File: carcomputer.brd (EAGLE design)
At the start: 103.8 x 90.2 mm, 73 parts, among them IC1 LM358N, K1 351, K2 RT184012, K3 RT184012, Q1 BS170, Q5 TIP136, T1 BC618, T2 BC618, T3 BC618, T4 BC618

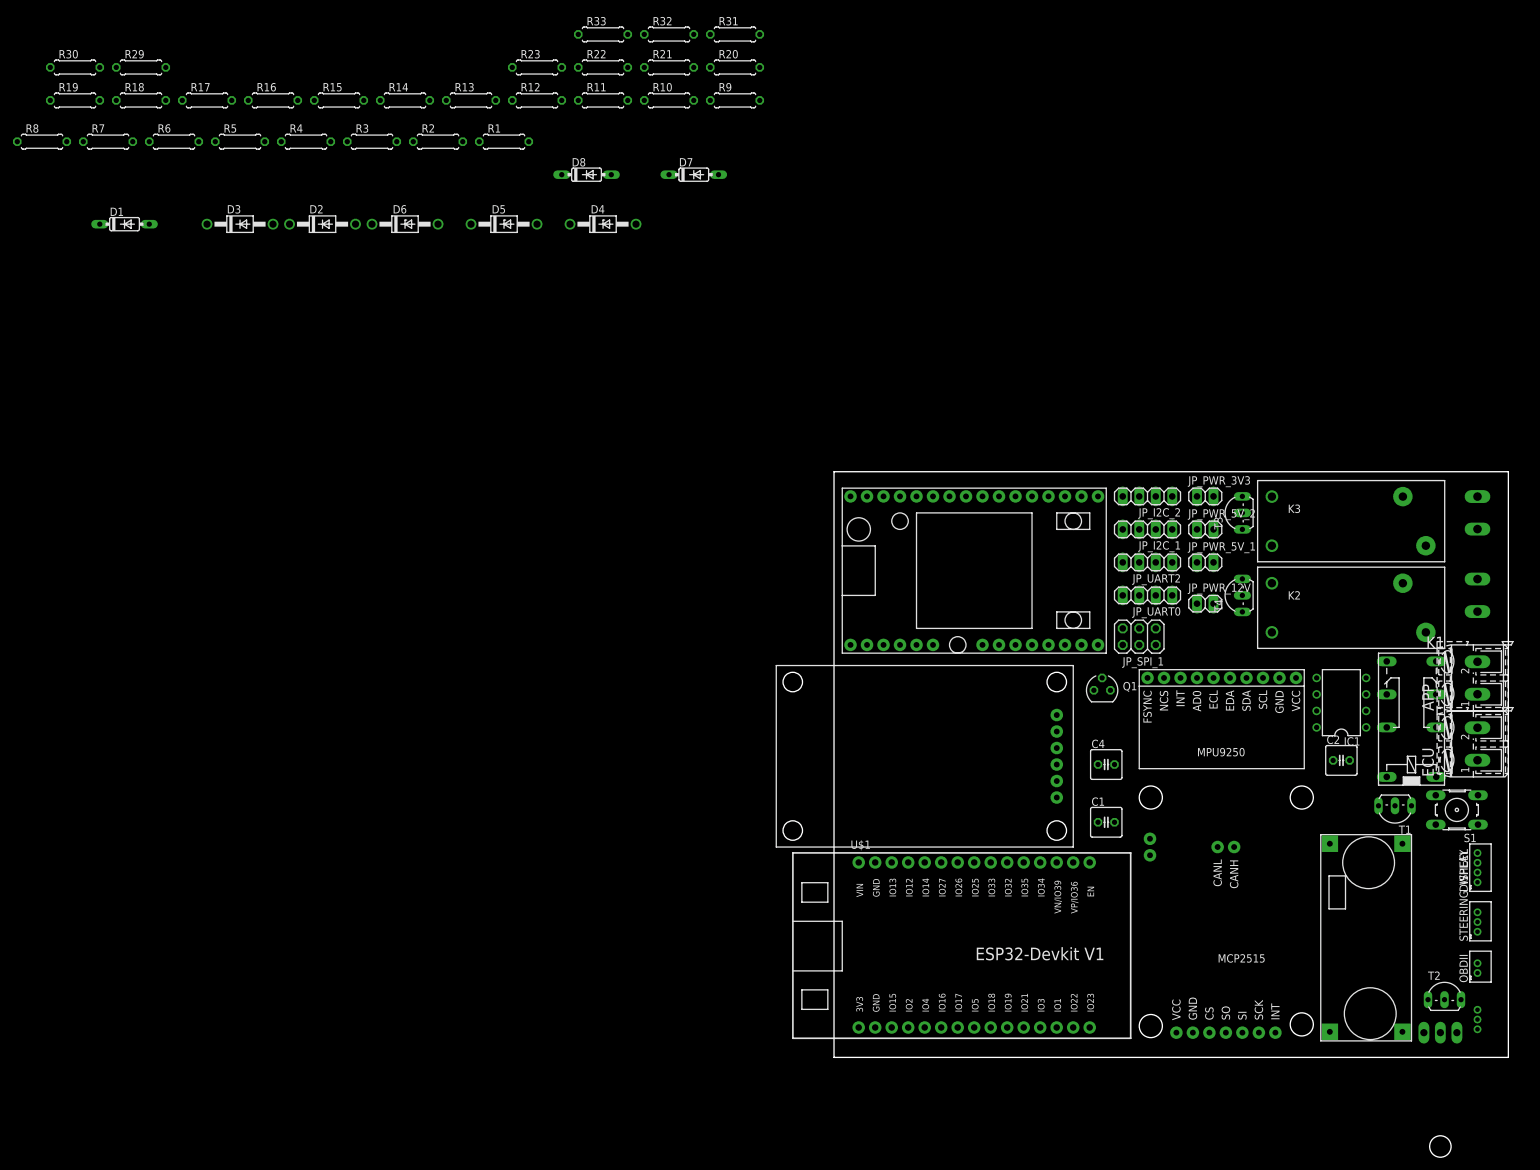
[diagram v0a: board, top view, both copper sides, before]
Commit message: Routed almost first complete single board
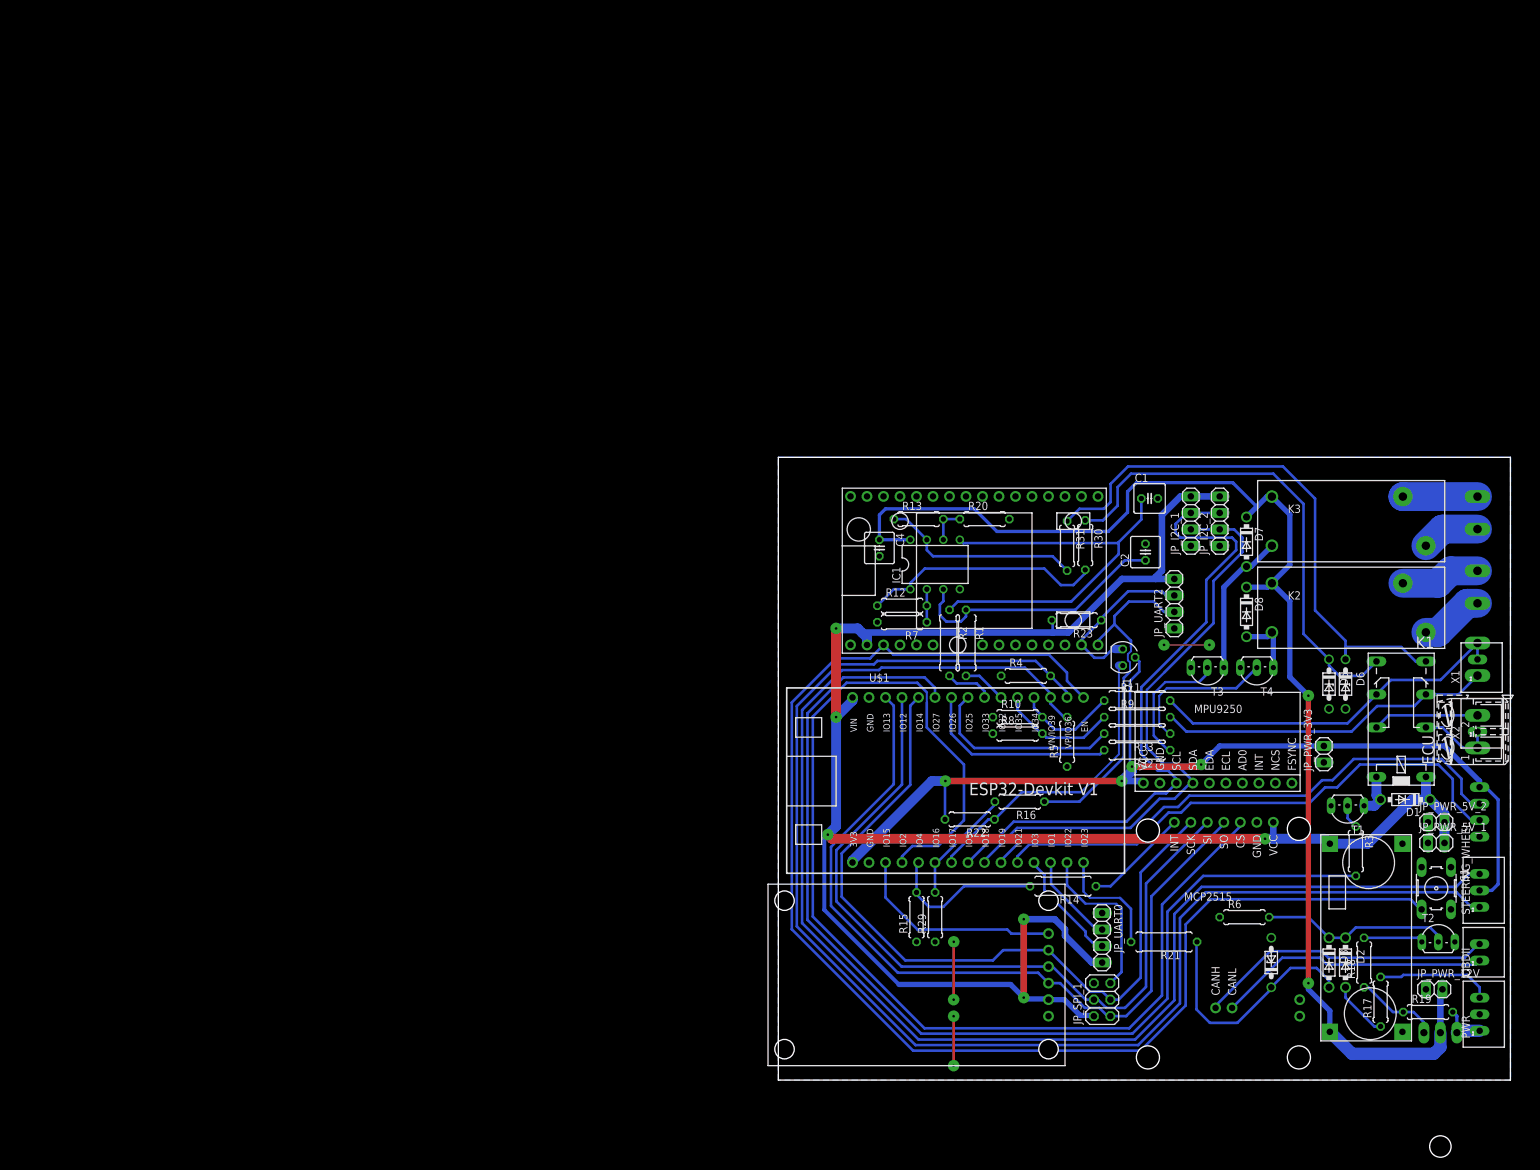
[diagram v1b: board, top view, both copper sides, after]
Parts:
- added X1, X2: 2.52B-ZR, con-jst-custom:B2B-ZR2.5
- D1, D7, D8: value 1N4148DO35-7 -> 1N40047; device diode:DO35-7 -> diode-custom:DO41-7.6
- D2, D3: value 1N4004 -> 1N40047; device diode:DO41-10 -> diode-custom:DO41-7.6
- D4, D5, D6: device diode:DO41Z10 -> diode-custom:DO41Z7.6
- DISPLAY: value B4B-ZR -> 2.54B-ZR; device con-jst-custom:B4B-ZR -> con-jst-custom:B4B-ZR2.5
- OBDII: value B2B-ZR -> 2.52B-ZR; device con-jst-custom:B2B-ZR -> con-jst-custom:B2B-ZR2.5
- PWR, STEERING_WHEEL: value B3B-ZR -> 2.53B-ZR; device con-jst-custom:B3B-ZR -> con-jst-custom:B3B-ZR2.5
- R1, R11, R14, R2, R21, R32, R33, R9: device rcl:0207/7 -> rcl:0309/10
- moved R19 251.1 mm to (88.9, 3.17)
- moved R18 230.4 mm to (79.1, 10.8), turned to 90 degrees
- moved R17 227.8 mm to (81.6, 4.76), turned to 90 degrees
- moved D1 216.2 mm to (85.4, 35.9), turned to 180 degrees
- moved R6 203.5 mm to (60.6, 17.8)
- moved D3 202.5 mm to (73.7, 10.8), turned to 270 degrees
- moved D2 194.2 mm to (76.2, 10.8), turned to 270 degrees
- moved R3 186.7 mm to (77.8, 27.9), turned to 270 degrees
- moved R29 179.0 mm to (13.0, 17.8), turned to 90 degrees
- moved R8 175.7 mm to (25.7, 46.0)
- moved R30 172.0 mm to (36.1, 75.1), turned to 270 degrees
- moved D6 161.2 mm to (76.2, 53.7), turned to 270 degrees
- moved R14 157.8 mm to (32.7, 22.5), turned to 180 degrees
- moved R16 157.7 mm to (26.0, 35.6), turned to 180 degrees
- moved R5 157.3 mm to (33.3, 44.8), turned to 90 degrees
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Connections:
- net +12V: now also PWR.1; no longer D7.C, D8.C, JP_PWR_12V.2, K2.A2, K3.A2, PWR.3
- net +3V3: now also DISPLAY.1; no longer DISPLAY.4
- net +5V: now also K1.1; no longer K1.16
- net APP_0_IN: now also X1.2
- net APP_1_IN: now also X1.1
- net BTN_0: now also R4.2, STEERING_WHEEL.1; no longer R5.2, STEERING_WHEEL.3
- net BTN_1: now also R5.2, STEERING_WHEEL.3; no longer R4.2, STEERING_WHEEL.1
- net GND: now also DISPLAY.4; no longer DISPLAY.1
- net GPS_RX: now also JP_UART2.3; no longer JP_UART2.2
- net GPS_TX: now also JP_UART2.2; no longer JP_UART2.3
- net I2C1_SCL: now also DISPLAY.2; no longer DISPLAY.3
- net I2C1_SDA: now also DISPLAY.3; no longer DISPLAY.2
- net IGNITION: now also PWR.3; no longer PWR.1
- net N$1: now also K1.16; no longer K1.1
- net N$6: now also K1.P2, X2.2; no longer K1.P1
- net N$7: now also K1.P1, X2.1; no longer K1.P2
- net PWR_IN+: now also D7.C, D8.C, JP_PWR_12V.2, K2.A2, K3.A2
- net UART0_RX: now also JP_UART0.3; no longer JP_UART0.2
- net UART0_TX: now also JP_UART0.2; no longer JP_UART0.3
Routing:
- net +5V: track 0.00 -> 314.1 mm, vias 0 -> 6
- net BTN_0: track 0.00 -> 212.2 mm
- net BTN_1: track 0.00 -> 210.4 mm
- net MCU_RESET: track 0.00 -> 209.9 mm
- net PWR_IN+: track 0.00 -> 200.7 mm, vias 0 -> 2
- net CAN_CS: track 0.00 -> 180.6 mm
- net APP_ENABLE: track 0.00 -> 165.4 mm
- net +3V3: track 0.00 -> 154.8 mm, vias 0 -> 4
- net SPI_MISO: track 0.00 -> 125.2 mm
- net SPI_MOSI: track 0.00 -> 120.6 mm
- net SPI_SCK: track 0.00 -> 118.0 mm
- net I2C0_SCL: track 0.00 -> 102.3 mm
- net I2C0_SDA: track 0.00 -> 93.7 mm
- net N$3: track 0.00 -> 87.2 mm
- net I2C1_SCL: track 0.00 -> 84.7 mm
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- added copper zone on layer 16, net GND
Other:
- board size 103.8 x 90.2 mm -> 112.7 x 95.9 mm

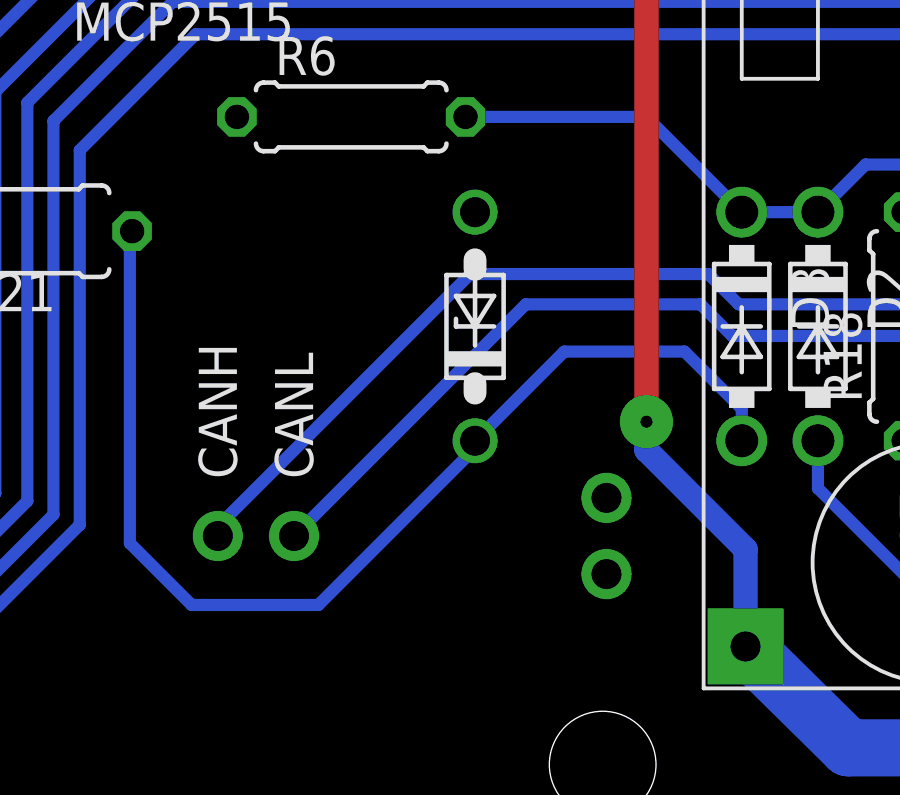
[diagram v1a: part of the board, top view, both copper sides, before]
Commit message: Added pinheaders connection for CAN terminator resistors
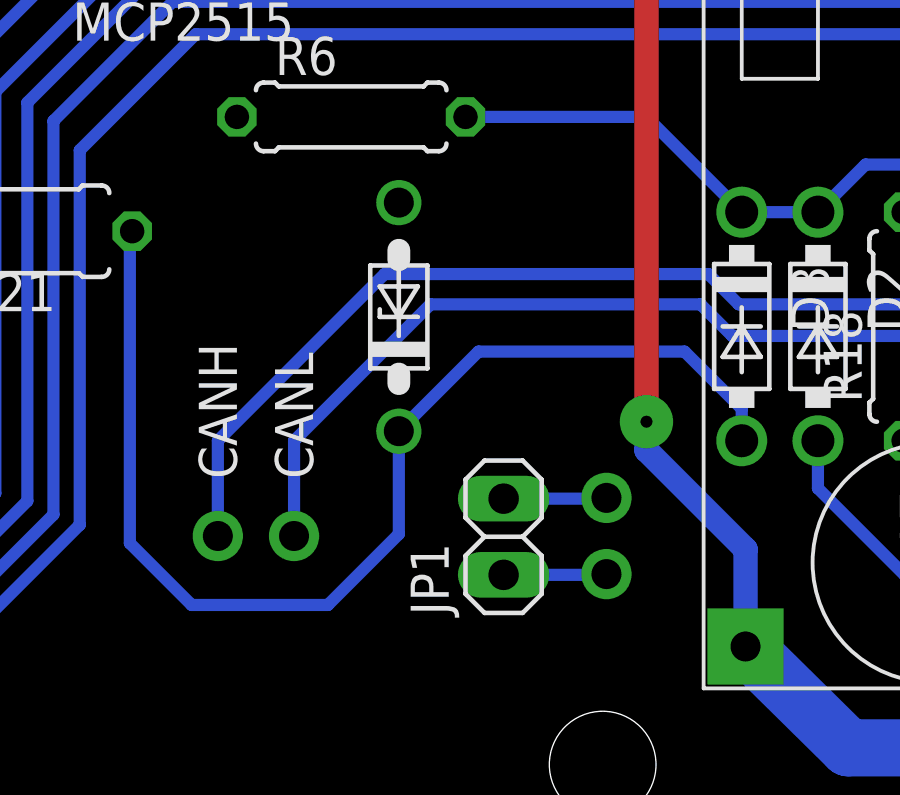
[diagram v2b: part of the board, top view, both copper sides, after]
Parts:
- added JP1: (no value), pinhead:1X02
- moved D4 2.56 mm to (62.2, 11.1)
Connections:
- new net CAN_TERM_RESTISTOR0: JP1.2, U$2.TERM_REST0
- new net CAN_TERM_RESTISTOR1: JP1.1, U$2.TERM_REST1
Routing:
- net CAN_TERM_RESTISTOR1: track 0.00 -> 3.44 mm
- net CAN_TERM_RESTISTOR0: track 0.00 -> 3.44 mm
- net CAN_L: track 42.0 -> 43.9 mm
- net N$11: track 37.2 -> 39.1 mm
- net CAN_H: track 45.7 -> 47.4 mm
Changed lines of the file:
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@@
 <setting verticaltext="up"/>
 </settings>
-<grid distance="4" unitdist="mil" unit="mil" style="lines" multiple="1" display="yes" altdistance="5" altunitdist="mil" altunit="mil"/>
+<grid distance="12.5" unitdist="mil" unit="mil" style="lines" multiple="1" display="yes" altdistance="5" altunitdist="mil" altunit="mil"/>
 <layers>
 <layer number="1" name="Top" color="4" fill="1" visible="yes" active="yes"/>
@@
 <layer number="19" name="Unrouted" color="6" fill="1" visible="yes" active="yes"/>
 <layer number="20" name="Dimension" color="24" fill="1" visible="no" active="yes"/>
-<layer number="21" name="tPlace" color="7" fill="1" visible="no" active="yes"/>
-<layer number="22" name="bPlace" color="7" fill="1" visible="no" active="yes"/>
-<layer number="23" name="tOrigins" color="15" fill="1" visible="no" active="yes"/>
-<layer number="24" name="bOrigins" color="15" fill="1" visible="no" active="yes"/>
-<layer number="25" name="tNames" color="7" fill="1" visible="no" active="yes"/>
-<layer number="26" name="bNames" color="7" fill="1" visible="no" active="yes"/>
-<layer number="27" name="tValues" color="7" fill="1" visible="no" active="yes"/>
-<layer number="28" name="bValues" color="7" fill="1" visible="no" active="yes"/>
+<layer number="21" name="tPlace" color="7" fill="1" visible="yes" active="yes"/>
+<layer number="22" name="bPlace" color="7" fill="1" visible="yes" active="yes"/>
+<layer number="23" name="tOrigins" color="15" fill="1" visible="yes" active="yes"/>
+<layer number="24" name="bOrigins" color="15" fill="1" visible="yes" active="yes"/>
+<layer number="25" name="tNames" color="7" fill="1" visible="yes" active="yes"/>
+<layer number="26" name="bNames" color="7" fill="1" visible="yes" active="yes"/>
+<layer number="27" name="tValues" color="7" fill="1" visible="yes" active="yes"/>
+<layer number="28" name="bValues" color="7" fill="1" visible="yes" active="yes"/>
 <layer number="29" name="tStop" color="7" fill="3" visible="no" active="yes"/>
 <layer number="30" name="bStop" color="7" fill="6" visible="no" active="yes"/>
@@
 <attribute name="VALUE" x="70.866" y="12.827" size="1.27" layer="27" ratio="10" rot="R270"/>
 </element>
-<element name="D4" library="diode-custom" package="DO41Z7.6" value="BZX83C3V6" x="64.77" y="10.795" smashed="yes" rot="R90">
-<attribute name="NAME" x="61.595" y="5.7785" size="1.27" layer="26" ratio="10" rot="MR0"/>
-<attribute name="VALUE" x="67.564" y="8.89" size="1.27" layer="27" ratio="10" rot="R90"/>
+<element name="D4" library="diode-custom" package="DO41Z7.6" value="BZX83C3V6" x="62.23" y="11.1125" smashed="yes" rot="R90">
+<attribute name="NAME" x="59.055" y="6.096" size="1.27" layer="26" ratio="10" rot="MR0"/>
+<attribute name="VALUE" x="65.024" y="9.2075" size="1.27" layer="27" ratio="10" rot="R90"/>
 </element>
 <element name="D5" library="diode-custom" package="DO41Z7.6" value="BZX83C5V1" x="73.66" y="53.6575" smashed="yes" rot="R270">
@@
 <attribute name="NAME" x="93.75" y="45.145" size="1.27" layer="25" rot="R90"/>
 <attribute name="VALUE" x="102.56" y="45.145" size="1.27" layer="27" rot="R90"/>
+</element>
+<element name="JP1" library="pinhead" library_urn="urn:adsk.eagle:library:325" package="1X02" package3d_urn="urn:adsk.eagle:package:22435/2" value="" x="65.7225" y="3.7846" smashed="yes" rot="R90">
+<attribute name="NAME" x="63.8937" y="1.1684" size="1.27" layer="25" ratio="10" rot="R90"/>
+<attribute name="POPULARITY" value="98" x="65.7225" y="3.7846" size="1.778" layer="27" rot="R90" display="off"/>
+<attribute name="VALUE" x="68.8975" y="1.2446" size="1.27" layer="27" rot="R90"/>
 </element>
 </elements>
@@
 <contactref element="U$2" pad="CAN_H"/>
 <contactref element="OBDII" pad="2"/>
-<wire x1="56.1975" y1="4.1275" x2="56.1975" y2="3.81" width="0.4064" layer="16"/>
+<wire x1="56.1975" y1="6.985" x2="56.1975" y2="3.81" width="0.4064" layer="16"/>
 <wire x1="96.8375" y1="13.6391" x2="96.6343" y2="13.6391" width="0.4064" layer="16"/>
 <wire x1="96.6343" y1="13.6391" x2="94.5268" y2="11.5316" width="0.4064" layer="16"/>
 <wire x1="73.5584" y1="11.5316" x2="72.54875" y2="12.54125" width="0.4064" layer="16"/>
-<wire x1="72.54875" y1="12.54125" x2="64.61125" y2="12.54125" width="0.4064" layer="16"/>
+<wire x1="72.54875" y1="12.54125" x2="61.75375" y2="12.54125" width="0.4064" layer="16"/>
 <wire x1="94.5268" y1="11.5316" x2="73.5584" y2="11.5316" width="0.4064" layer="16"/>
-<wire x1="64.61125" y1="12.54125" x2="56.1975" y2="4.1275" width="0.4064" layer="16"/>
+<wire x1="61.75375" y1="12.54125" x2="56.1975" y2="6.985" width="0.4064" layer="16"/>
 </signal>
 <signal name="CAN_L">
@@
 <wire x1="96.2173" y1="10.4775" x2="73.3425" y2="10.4775" width="0.4064" layer="16"/>
 <wire x1="73.3425" y1="10.4775" x2="72.2884" y2="11.5316" width="0.4064" layer="16"/>
-<wire x1="72.2884" y1="11.5316" x2="66.4591" y2="11.5316" width="0.4064" layer="16"/>
-<wire x1="66.4591" y1="11.5316" x2="58.7375" y2="3.81" width="0.4064" layer="16"/>
+<wire x1="72.2884" y1="11.5316" x2="63.2841" y2="11.5316" width="0.4064" layer="16"/>
+<wire x1="63.2841" y1="11.5316" x2="58.7375" y2="6.985" width="0.4064" layer="16"/>
+<wire x1="58.7375" y1="6.985" x2="58.7375" y2="3.81" width="0.4064" layer="16"/>
 </signal>
 <signal name="I2C0_SDA">
@@
 <contactref element="D4" pad="C"/>
 <contactref element="R21" pad="1"/>
-<wire x1="64.77" y1="6.985" x2="64.77" y2="6.73218125" width="0.4064" layer="16"/>
-<wire x1="64.77" y1="6.73218125" x2="59.54911875" y2="1.5113" width="0.4064" layer="16"/>
+<wire x1="62.23" y1="7.3025" x2="62.23" y2="3.87468125" width="0.4064" layer="16"/>
+<wire x1="62.23" y1="3.87468125" x2="59.86661875" y2="1.5113" width="0.4064" layer="16"/>
 <wire x1="53.34" y1="13.97" x2="53.2638" y2="13.97" width="0.4064" layer="16"/>
 <wire x1="53.2638" y1="13.97" x2="53.2638" y2="3.56988125" width="0.4064" layer="16"/>
 <wire x1="53.2638" y1="3.56988125" x2="55.32238125" y2="1.5113" width="0.4064" layer="16"/>
-<wire x1="55.32238125" y1="1.5113" x2="59.54911875" y2="1.5113" width="0.4064" layer="16"/>
+<wire x1="55.32238125" y1="1.5113" x2="59.86661875" y2="1.5113" width="0.4064" layer="16"/>
 <wire x1="73.66" y1="6.985" x2="73.66" y2="8.0518" width="0.4064" layer="16"/>
 <wire x1="73.66" y1="8.0518" x2="71.755" y2="9.9568" width="0.4064" layer="16"/>
-<wire x1="67.7418" y1="9.9568" x2="64.77" y2="6.985" width="0.4064" layer="16"/>
-<wire x1="71.755" y1="9.9568" x2="67.7418" y2="9.9568" width="0.4064" layer="16"/>
+<wire x1="64.8843" y1="9.9568" x2="62.23" y2="7.3025" width="0.4064" layer="16"/>
+<wire x1="71.755" y1="9.9568" x2="64.8843" y2="9.9568" width="0.4064" layer="16"/>
 </signal>
 <signal name="N$8">
@@
 <wire x1="96.52" y1="46.3402" x2="96.52" y2="43.8404" width="0.4064" layer="16"/>
 </signal>
+<signal name="CAN_TERM_RESTISTOR0">
+<contactref element="U$2" pad="TERM_REST0"/>
+<contactref element="JP1" pad="2"/>
+<wire x1="69.1515" y1="5.08" x2="69.1261" y2="5.0546" width="0.4064" layer="16"/>
+<wire x1="69.1261" y1="5.0546" x2="65.7225" y2="5.0546" width="0.4064" layer="16"/>
+</signal>
+<signal name="CAN_TERM_RESTISTOR1">
+<contactref element="U$2" pad="TERM_REST1"/>
+<contactref element="JP1" pad="1"/>
+<wire x1="69.1515" y1="2.54" x2="69.1261" y2="2.5146" width="0.4064" layer="16"/>
+<wire x1="69.1261" y1="2.5146" x2="65.7225" y2="2.5146" width="0.4064" layer="16"/>
+</signal>
 </signals>
